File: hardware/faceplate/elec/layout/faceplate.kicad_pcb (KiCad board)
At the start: 2 copper layers, 181.9 x 128 mm, 70 parts

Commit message: production check command and fixes coming out of that
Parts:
- moved SO5 4.36 mm to (7.96, 16.1)
- moved SW35 4.34 mm to (7.00, 45.2)
- moved SW33 4.34 mm to (7.00, 23.8)
- moved SW34 4.34 mm to (7.00, 34.5)
- moved SW36 4.34 mm to (7.00, 55.9)
- moved SO6 2.46 mm to (7.96, 114.0)
- moved SLOT4 0.88 mm to (175.1, 125.0)
- moved SLOT2 0.72 mm to (175.1, 3.00)
- moved SLOT3 0.50 mm to (7.50, 125.0)
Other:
- board size 181.9 x 128 mm -> 182.6 x 128.5 mm

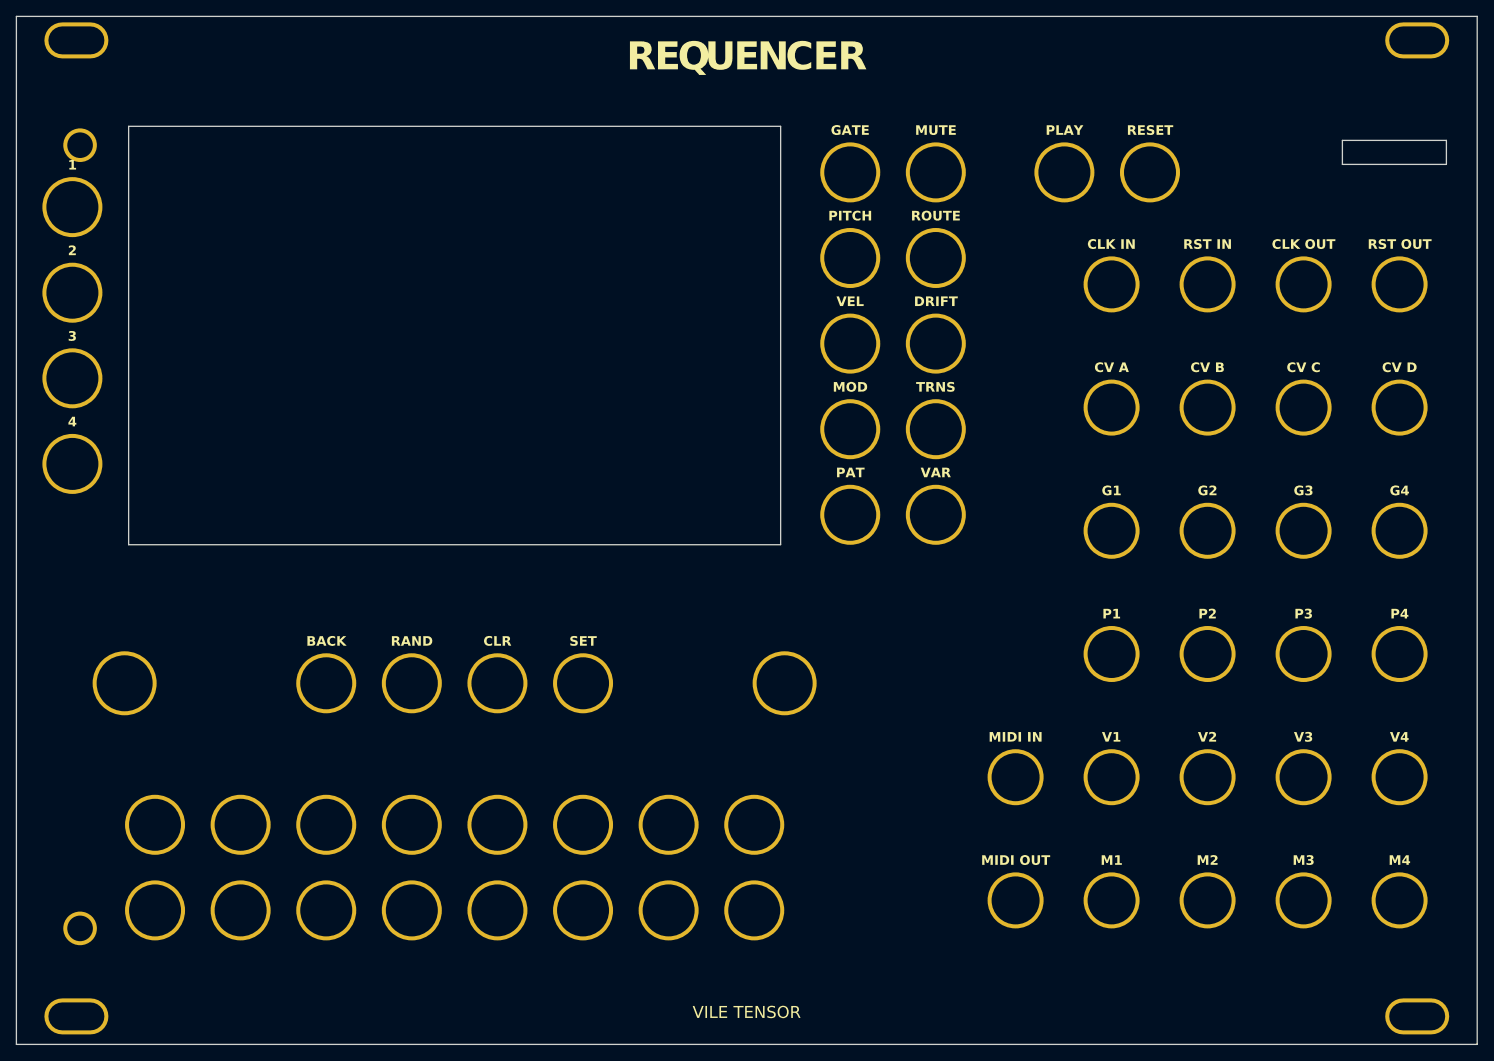
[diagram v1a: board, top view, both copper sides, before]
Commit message: Increase cutouts for encoders & jacks
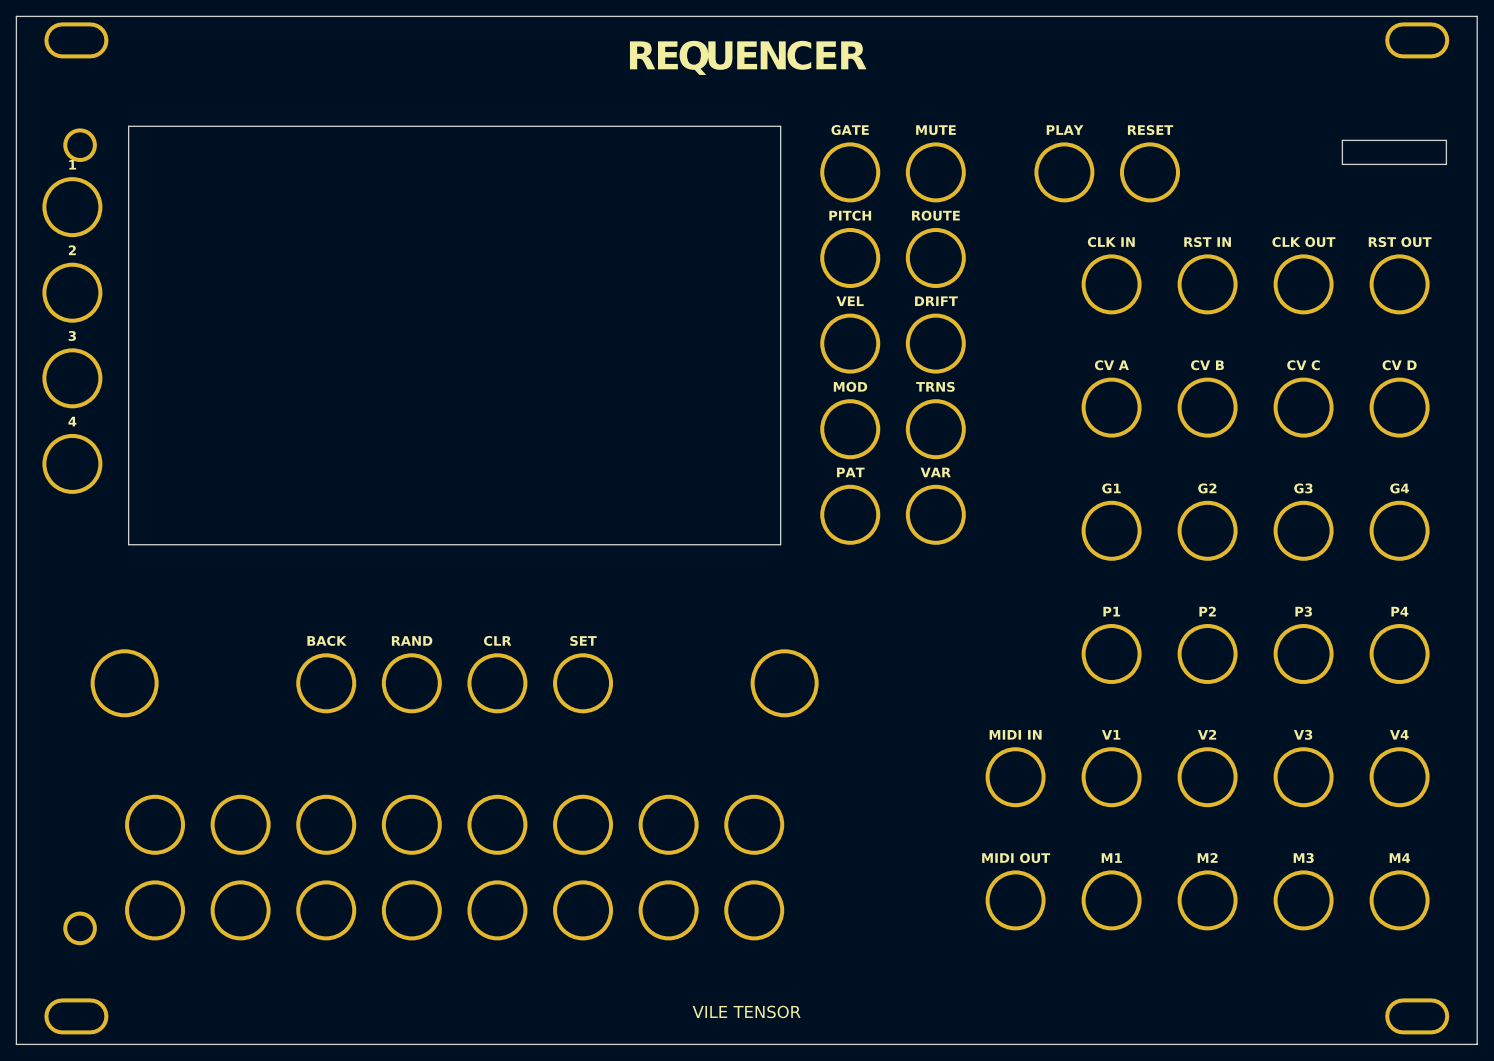
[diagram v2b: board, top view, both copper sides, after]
